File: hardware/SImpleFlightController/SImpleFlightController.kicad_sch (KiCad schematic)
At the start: 0 parts

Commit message: updated schematics
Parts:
- added C1, C28, C29, C30: 1uF, Capacitor_SMD:C_0402_1005Metric, symbol Device:C
- added C10, C11, C13: 22uF, Capacitor_SMD:C_0805_2012Metric, symbol Device:C
- added C12, C2, C9: 10uF, Capacitor_SMD:C_0603_1608Metric, symbol Device:C
- added C14: 100uF, Capacitor_SMD:C_0201_0603Metric, symbol Device:C
- added C15, C19, C20, C21, C22, C23, C24, C25, C26, C27, C37: 100nF, Capacitor_SMD:C_0201_0603Metric, symbol Device:C
- added C16: 2.2uF, Capacitor_SMD:C_0603_1608Metric, symbol Device:C
- added C17, C18: 22uF, Capacitor_SMD:C_0402_1005Metric, symbol Device:C
- added C3, C31, C5: 10uF, Capacitor_SMD:C_0402_1005Metric, symbol Device:C
- added C32: 2.2uF, Capacitor_SMD:C_0201_0603Metric, symbol Device:C
- added C33, C34: 20pF, Capacitor_SMD:C_0201_0603Metric, symbol Device:C
- added C35, C36: 6.8pF, Capacitor_SMD:C_0201_0603Metric, symbol Device:C
- added C4: 47nF, Capacitor_SMD:C_0201_0603Metric, symbol Device:C
- added C6: 44uF, Capacitor_SMD:C_0603_1608Metric, symbol Device:C
- added C7, C8: 10uF, Capacitor_SMD:C_0805_2012Metric, symbol Device:C
- added Card1: TF-01A, lcsc:TF-SMD_TF-01A, symbol lcsc:TF-01A
- added D1: LED, LED_SMD:LED_0402_1005Metric, symbol Device:LED
- added J1: Screw_Terminal_01x02, TerminalBlock:TerminalBlock_Xinya_XY308-2.54-2P_1x02_P2.54mm_Horizontal, symbol Connector:Screw_Terminal_01x02
- added J2, J3: Conn_01x03, Connector_PinHeader_2.54mm:PinHeader_1x03_P2.54mm_Vertical, symbol Connector_Generic:Conn_01x03
- added L1: 1uH, lcsc:L2520, symbol lcsc:DFE252012F-1R0M=P2
- added L2: 1.5uH, lcsc:IND-SMD_L4.0-W4.0-A, symbol Device:L
- added L3: 5.6uH, lcsc:IND-SMD_L3.0-W3.0, symbol Device:L
- added L4: FCM1608KF-601T03, lcsc:L0603, symbol lcsc:FCM1608KF-601T03
- added R1, R2: 5.1K, Resistor_SMD:R_0201_0603Metric, symbol Device:R
- added R10, R11, R12, R13, R16, R17, R18, R19, R20, R21, R22, R6, R7, R8, R9: 10K, Resistor_SMD:R_0201_0603Metric, symbol Device:R
- added R14: 100K, Resistor_SMD:R_0402_1005Metric, symbol Device:R
- added R15: 22.1K, Resistor_SMD:R_0402_1005Metric, symbol Device:R
- added R3: 383, Resistor_SMD:R_0201_0603Metric, symbol Device:R
- added R4: 5.23K, Resistor_SMD:R_0201_0603Metric, symbol Device:R
- added R5: 30.1K, Resistor_SMD:R_0201_0603Metric, symbol Device:R
- added SW1, SW2: TS-1088-AR02016, lcsc:SW-SMD_L3.9-W3.0-P4.45, symbol lcsc:TS-1088-AR02016
- added U1: BQ25883RGER, lcsc:VFQFPN-24_L4.0-W4.0-P0.50-BL-EP2.8, symbol lcsc:BQ25883RGER
- added U2: ICM-45686, lcsc:LGA-14_L3.0-W2.5-P0.50-TL, symbol lcsc:ICM-45686
- added U3: STM32F722RETx, Package_QFP:LQFP-64_10x10mm_P0.5mm, symbol MCU_ST_STM32F7:STM32F722RETx
- added U4: BMP580, lcsc:LGA-10_L2.0-W2.0-P0.50-TL_BMP580, symbol lcsc:BMP580
- added U5: TPS63070RNMR, lcsc:VQFN-HR-15_L3.0-W2.5-P0.50-BL_TPS63070RNMR, symbol lcsc:TPS63070RNMR
- added U6: LMR51430, Package_TO_SOT_SMD:SOT-23-6, symbol Regulator_Switching:LMR51430
- added USB1: TYPE-C 16PIN 2MD(073), lcsc:USB-C-SMD_TYPE-C-6PIN-2MD-073, symbol lcsc:TYPE-C16PIN2MD(073)
- added X1: X322525MOB4SI, lcsc:CRYSTAL-SMD_4P-L3.2-W2.5-BL, symbol lcsc:X322525MOB4SI
- added X2: Q13FC1350000400, lcsc:FC-135R_L3.2-W1.5, symbol lcsc:Q13FC1350000400
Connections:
- new net: C4.2, U1.12 (BTST)
- new net: D1.1 (K), U1.2 (STAT)
- new net: C5.1, L1.2, U1.21 (PMID), U1.22 (PMID)
- new net: R6.2, U1.7 (TS)
- new net: R3.2, U1.8 (ILIM)
- new net: D1.2 (A), R7.1
- new net: C32.1, U3.30 (VCAP_1)
- new net: L2.1, U5.11 (L1)
- new net: L2.2, U5.9 (L2)
- new net: R2.2, USB1.10 (CC2)
- new net: R1.2, USB1.4 (CC1)
- new net: L4.1, U3.13 (VDDA)
- new net: R13.2, U5.2 (PG)
- new net: R14.1, R15.2, U6.4 (FB)
- new net: C15.2, L3.1, R14.2, U6.2 (SW)
- new net: R12.2, U5.1 (PS/SYNC), U5.14 (EN)
- new net: C14.2, U5.3 (Vaux)
- new net: R4.1, R5.2
- new net: C15.1, U6.6 (CB)
- new net +3V3: C17.1, C18.1, C19.1, C20.1, C21.1, C22.1, C23.1, C24.1, C25.1, C26.1, C27.1, C28.1, C29.1, C30.1, C31.1, Card1.4 (VDD), L3.2, L4.2, R10.2, R11.2, R16.2, R17.2, R18.2, R19.2, R20.2, R21.2, R7.2, R8.2, R9.2, SW2.1, U2.5 (VDDIO), U2.8 (VDD), U3.1 (VBAT), U3.19 (VDD), U3.32 (VDD), U3.48 (VDD), U3.64 (VDD), U4.1 (VDDIO), U4.10 (VDD)
- new net +5V: C10.1, C11.1, C12.1, C13.1, J2.1 (Pin_1), J3.1 (Pin_1), R13.1, U5.5 (FB), U5.7 (Vout), U5.8 (Vout)
- new net BAT+: C2.1, J1.1 (Pin_1), U1.13 (BAT), U1.14 (BAT)
- new net BMP_INT: U4.7 (INT)
- new net BOOT: R22.2, SW2.2, U3.60 (BOOT0)
- new net BQ_CE: U1.3 (~{CE}), U3.61 (PB8)
- new net BQ_INT: R11.1, U1.6 (~{INT}), U3.57 (PB5), U3.62 (PB9)
- new net BQ_PG: R8.1, U1.9 (~{PG})
- new net BTST: C4.1, L1.1, U1.17 (SW), U1.18 (SW)
- new net GND: C10.2, C11.2, C12.2, C13.2, C14.1, C16.2, C17.2, C18.2, C19.2, C2.2, C20.2, C21.2, C22.2, C23.2, C24.2, C25.2, C26.2, C27.2, C28.2, C29.2, C3.2, C30.2, C31.2, C32.2, C33.2, C34.2, C35.2, C36.2, C37.1, C5.2, C6.2, C7.2, C8.2, C9.2, Card1.10 (GND), Card1.11 (GND), Card1.12 (GND), Card1.13 (GND), Card1.6 (VSS), J2.3 (Pin_3), J3.3 (Pin_3), R1.1, R15.1, R2.1, R22.1, R3.1, R5.1, R6.1, SW1.1, U1.19 (GND), U1.20 (GND), U2.6 (GND), U3.12 (VSSA), U3.18 (VSS), U3.31 (VSS), U3.47 (VSS), U3.63 (VSS), U4.3 (VSS), U4.5 (SDO), U4.6 (CSB), U4.8 (VSS), U4.9 (VSS), U5.10 (PGND), U5.15 (Vsel), U5.4 (GND), U5.6 (FB2), U6.1 (GND), USB1.1 (GND), USB1.12 (GND), USB1.13 (SHELL), USB1.14 (SHELL), X1.2 (GND), X1.4 (GND)
- new net HSE_IN: C33.1, U3.5 (PH0), X1.1 (OSC1)
- new net HSE_OUT: C34.1, U3.6 (PH1), X1.3 (OSC2)
- new net I2C_SCL: R10.1, U1.5 (SCL), U3.58 (PB6), U4.2 (SCK)
- new net I2C_SDA: R9.1, U1.4 (SDA), U3.59 (PB7), U4.4 (SDI)
- new net ICM_CS: U2.12 (AP_CS), U3.20 (PA4)
- new net ICM_INT1: U2.4 (INT1/INT), U3.24 (PC4), U3.41 (PA8)
- new net ICM_INT2: U2.9 (INT2/FSYNC/CLKIN), U3.25 (PB0), U3.42 (PA9)
- new net ICM_SCK: U2.13 (AP_SCL/AP_SCLK), U3.21 (PA5)
- new net ICM_SDI: U2.14 (AP_SDA/AP_SDIO/AP_SDI), U3.23 (PA7)
- new net ICM_SDO: U2.1 (AP_SDO/AP_AD0), U3.22 (PA6)
- new net LSE_IN: C35.1, U3.3 (PC14), X2.1
- new net LSE_OUT: C36.1, U3.4 (PC15), X2.2
- new net PGND: C1.2, J1.2 (Pin_2)
- new net RESET: C37.2, SW1.2, U3.7 (NRST)
- new net SD_CD: Card1.9 (CD), U3.55 (PB3)
- new net SD_CLK: Card1.5 (CLK(SCLK)), R21.1, U3.53 (PC12)
- new net SD_CMD: Card1.3 (CMD(DI)), R20.1, U3.54 (PD2)
- new net SD_DAT0: Card1.7 (DAT0(D0)), R16.1, U3.39 (PC8)
- new net SD_DAT1: Card1.8 (DAT1(RSV)), R17.1, U3.40 (PC9)
- new net SD_DAT2: Card1.1 (DAT2(RSV)), R18.1, U3.51 (PC10)
- new net SD_DAT3: Card1.2 (CDDAT3(CS)), R19.1, U3.52 (PC11)
- new net SERVO1: J2.2 (Pin_2), U3.14 (PA0)
- new net SERVO2: J3.2 (Pin_2), U3.15 (PA1)
- new net USB_DN: U3.44 (PA11), USB1.5 (DN2), USB1.7 (DN1)
- new net USB_DP: U3.45 (PA12), USB1.6 (DP1), USB1.8 (DP2)
- new net VBUS: C1.1, U1.23 (VBUS), USB1.11 (VBUS), USB1.2 (VBUS)
- new net VREGN: C3.1, R4.2, U1.11 (REGN)
- new net VSYS: C16.1, C6.1, C7.1, C8.1, C9.1, R12.1, U1.15 (SYS), U1.16 (SYS), U5.12 (Vin), U5.13 (Vin), U6.3 (VIN), U6.5 (EN)
- no-connect marks 0 -> 33

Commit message: added local files
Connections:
- net at U1.2 (STAT): now also D1.2 (A); no longer D1.1 (K)
- net at R7.1: now also D1.1 (K); no longer D1.2 (A)
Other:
- moved on the sheet: D1
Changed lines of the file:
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@@
 	(symbol
 		(lib_id "Device:LED")
-		(at 78.74 171.45 180)
+		(at 78.74 171.45 0)
 		(unit 1)
 		(exclude_from_sim no)
@@
 		(dnp no)
 		(property "Reference" "D1"
-			(at 76.2 172.466 0)
+			(at 81.28 170.434 0)
 			(effects
 				(font
@@
 		)
 		(property "Value" "LED"
-			(at 78.74 174.244 0)
+			(at 78.74 168.656 0)
 			(effects
 				(font

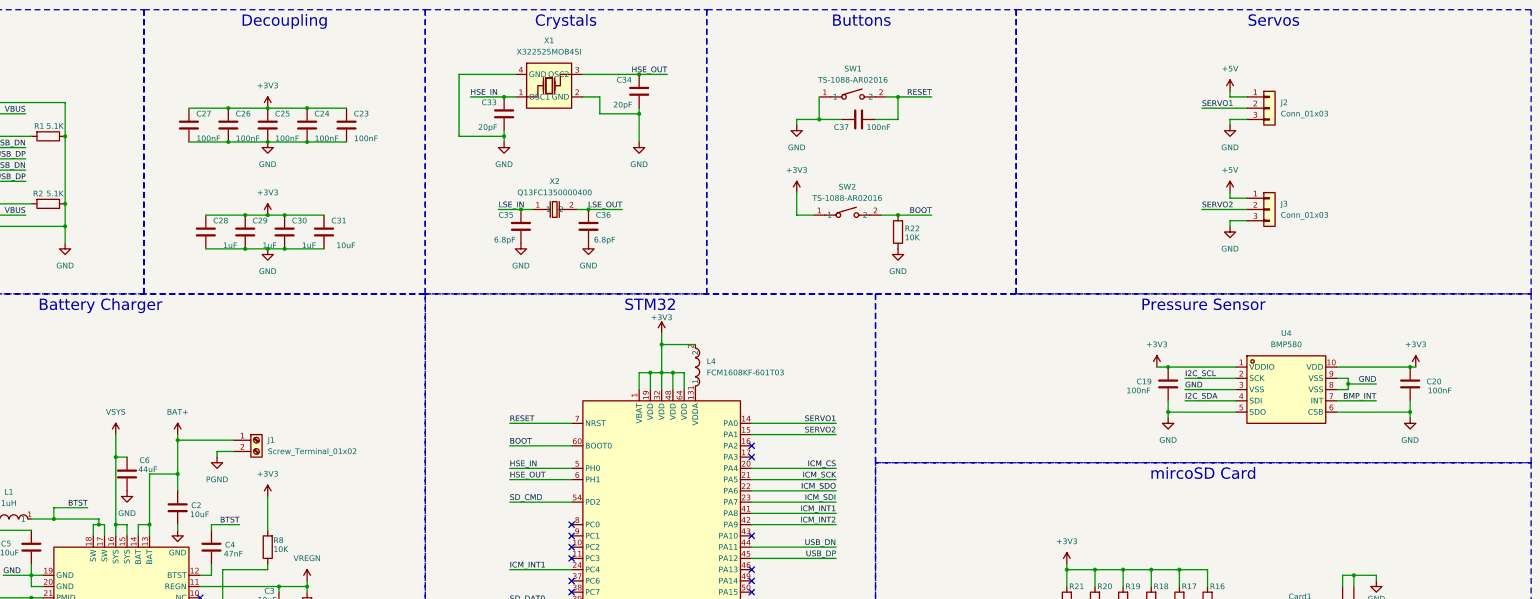
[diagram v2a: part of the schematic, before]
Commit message: updated GPS to front
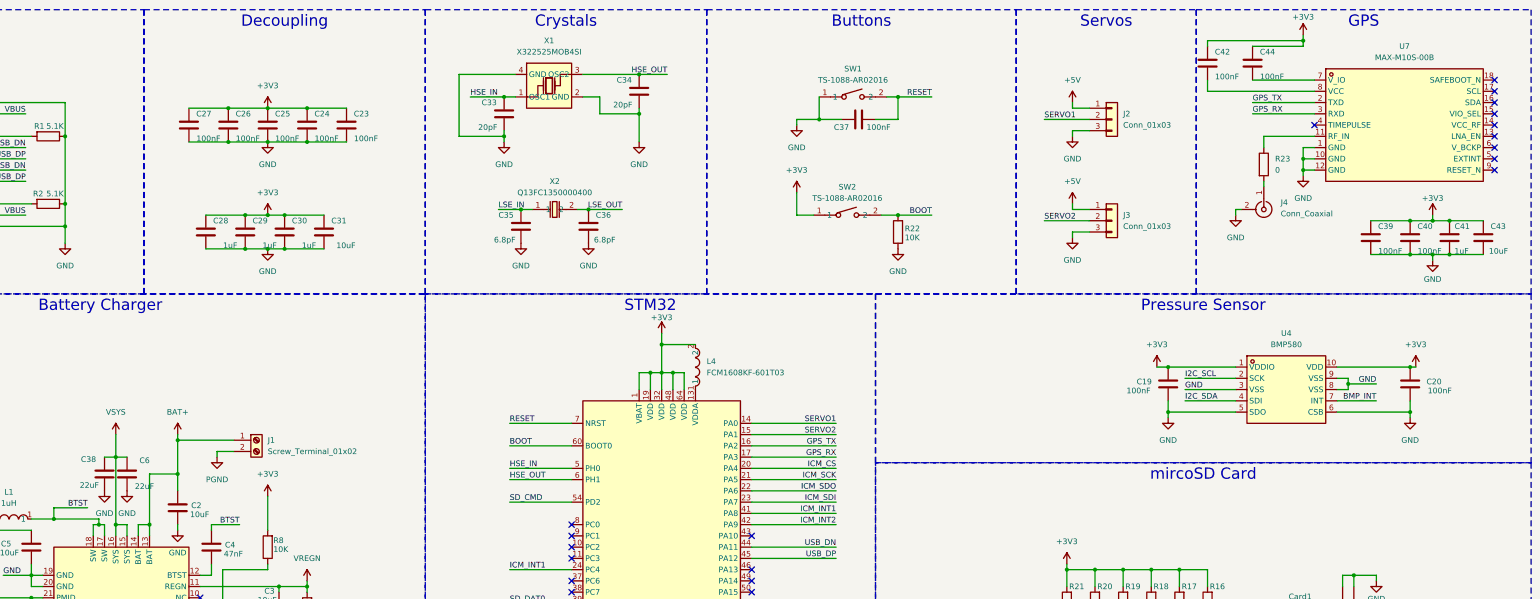
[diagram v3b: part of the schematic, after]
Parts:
- added C38: 22uF, Capacitor_SMD:C_0603_1608Metric, symbol Device:C
- added C39, C40, C42, C44: 100nF, Capacitor_SMD:C_0402_1005Metric, symbol Device:C
- added C41: 1uF, Capacitor_SMD:C_0402_1005Metric, symbol Device:C
- added C43: 10uF, Capacitor_SMD:C_0402_1005Metric, symbol Device:C
- added J4: Conn_Coaxial, Connector_Coaxial:U.FL_Hirose_U.FL-R-SMT-1_Vertical, symbol Connector:Conn_Coaxial
- added R23: 0, Resistor_SMD:R_0201_0603Metric, symbol Device:R
- added U7: MAX-M10S-00B, lcsc:SMD-18_L10.1-W9.7-P1.10-TL_SKG09F, symbol lcsc:MAX-M10S-00B
- C6: value 44uF -> 22uF
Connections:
- net +3V3: now also C39.1, C40.1, C41.1, C42.1, C43.1, C44.1
- net GND: now also C38.2, C39.2, C40.2, C41.2, C43.2, J4.2 (Ext), U7.1 (GND), U7.10 (GND), U7.12 (GND)
- net VSYS: now also C38.1
- net GPS_TX: now reaches U3.16 (PA2)
- net GPS_TX: now also U7.2 (TXD)
- net GPS_RX: now reaches U3.17 (PA3)
- net GPS_RX: now also U7.3 (RXD)
- new net: J4.1 (In), R23.2
- new net: C42.2, U7.8 (VCC)
- new net: R23.1, U7.11 (RF_IN)
- new net: C44.2, U7.7 (V_IO)
- no-connect marks 33 -> 41
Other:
- moved on the sheet: J2, J3
